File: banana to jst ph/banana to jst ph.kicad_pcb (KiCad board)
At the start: 2 copper layers, 34.3 x 26.6 mm, 32 parts, among them J1 USB4125-GF-A-0190, J2 Positive, J3 Negative

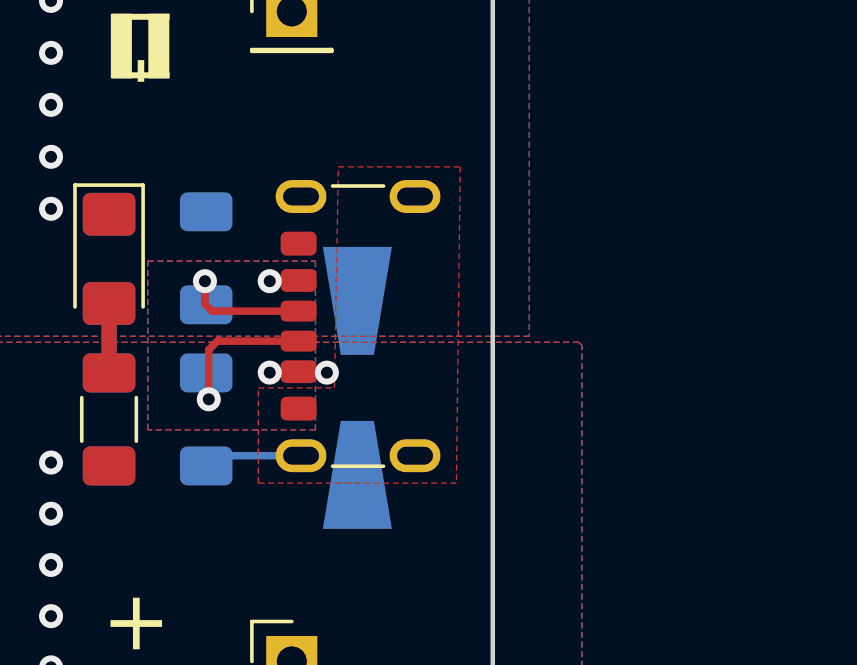
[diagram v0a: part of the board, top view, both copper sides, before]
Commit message: updated schematic but need to verify pin 1 and 2 connections
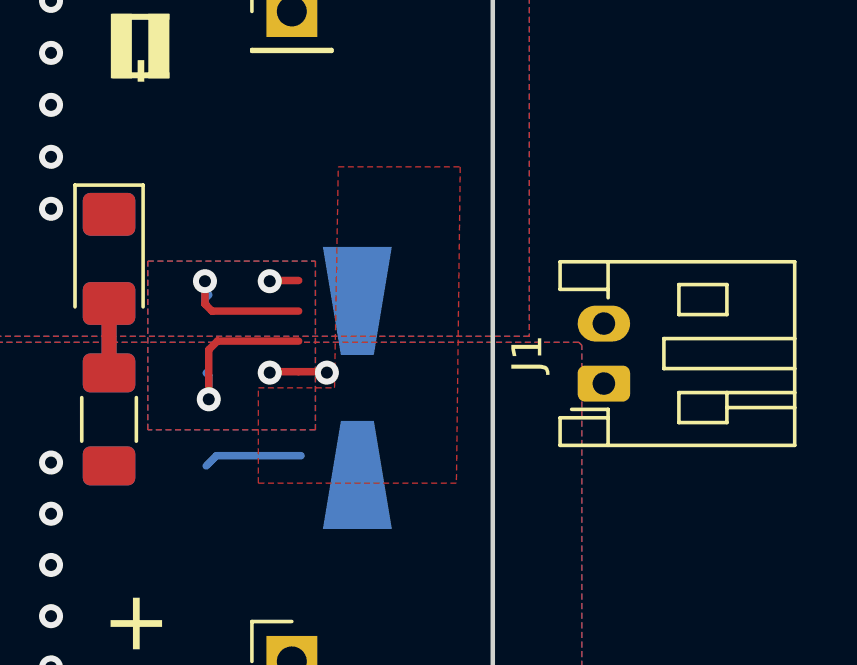
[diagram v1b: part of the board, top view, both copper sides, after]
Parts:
- removed R3, R4: 5k1, Resistor_SMD:R_1206_3216Metric_Pad1.30x1.75mm_HandSolder
- J1: value USB4125-GF-A-0190 -> LiPo JST PH [VERIFY]; footprint Connector_USB:USB_C_Receptacle_GCT_USB4125-xx-x_6P_TopMnt_Horizontal -> Connector_JST:JST_PH_S2B-PH-K_1x02_P2.00mm_Horizontal
- moved J1 7.35 mm to (163.3, 101.1)
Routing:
- net (no net): track 0.00 -> 10.6 mm, vias 0 -> 2
- net Net-(J1-CC1): track 5.68 -> 0.00 mm, vias 1 -> 0
- net Net-(J1-CC2): track 4.91 -> 0.00 mm, vias 1 -> 0

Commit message: jst ph sm4 adapter rev 2 ready for fab
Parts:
- J1: value LiPo JST PH [VERIFY] -> JST S2B-PH-SM4; footprint Connector_JST:JST_PH_S2B-PH-K_1x02_P2.00mm_Horizontal -> Connector_JST:JST_PH_S2B-PH-SM4-TB_1x02-1MP_P2.00mm_Horizontal
- moved J1 8.73 mm to (154.7, 99.6)
- moved D3 1.65 mm to (155.1, 99.6)
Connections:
- J1 pad 1: GND -> /Positive
- J1 pad 2: /Positive -> GND
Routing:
- net (no net): track 10.6 -> 0.00 mm, vias 2 -> 0
- net GND: track 8.90 -> 5.60 mm
- net /Positive: track 2.90 -> 0.00 mm, vias 9 -> 6
